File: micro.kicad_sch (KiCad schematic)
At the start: 23 parts, among them U10 RP2040, U11 W25Q128JVS, Y2 12MHz

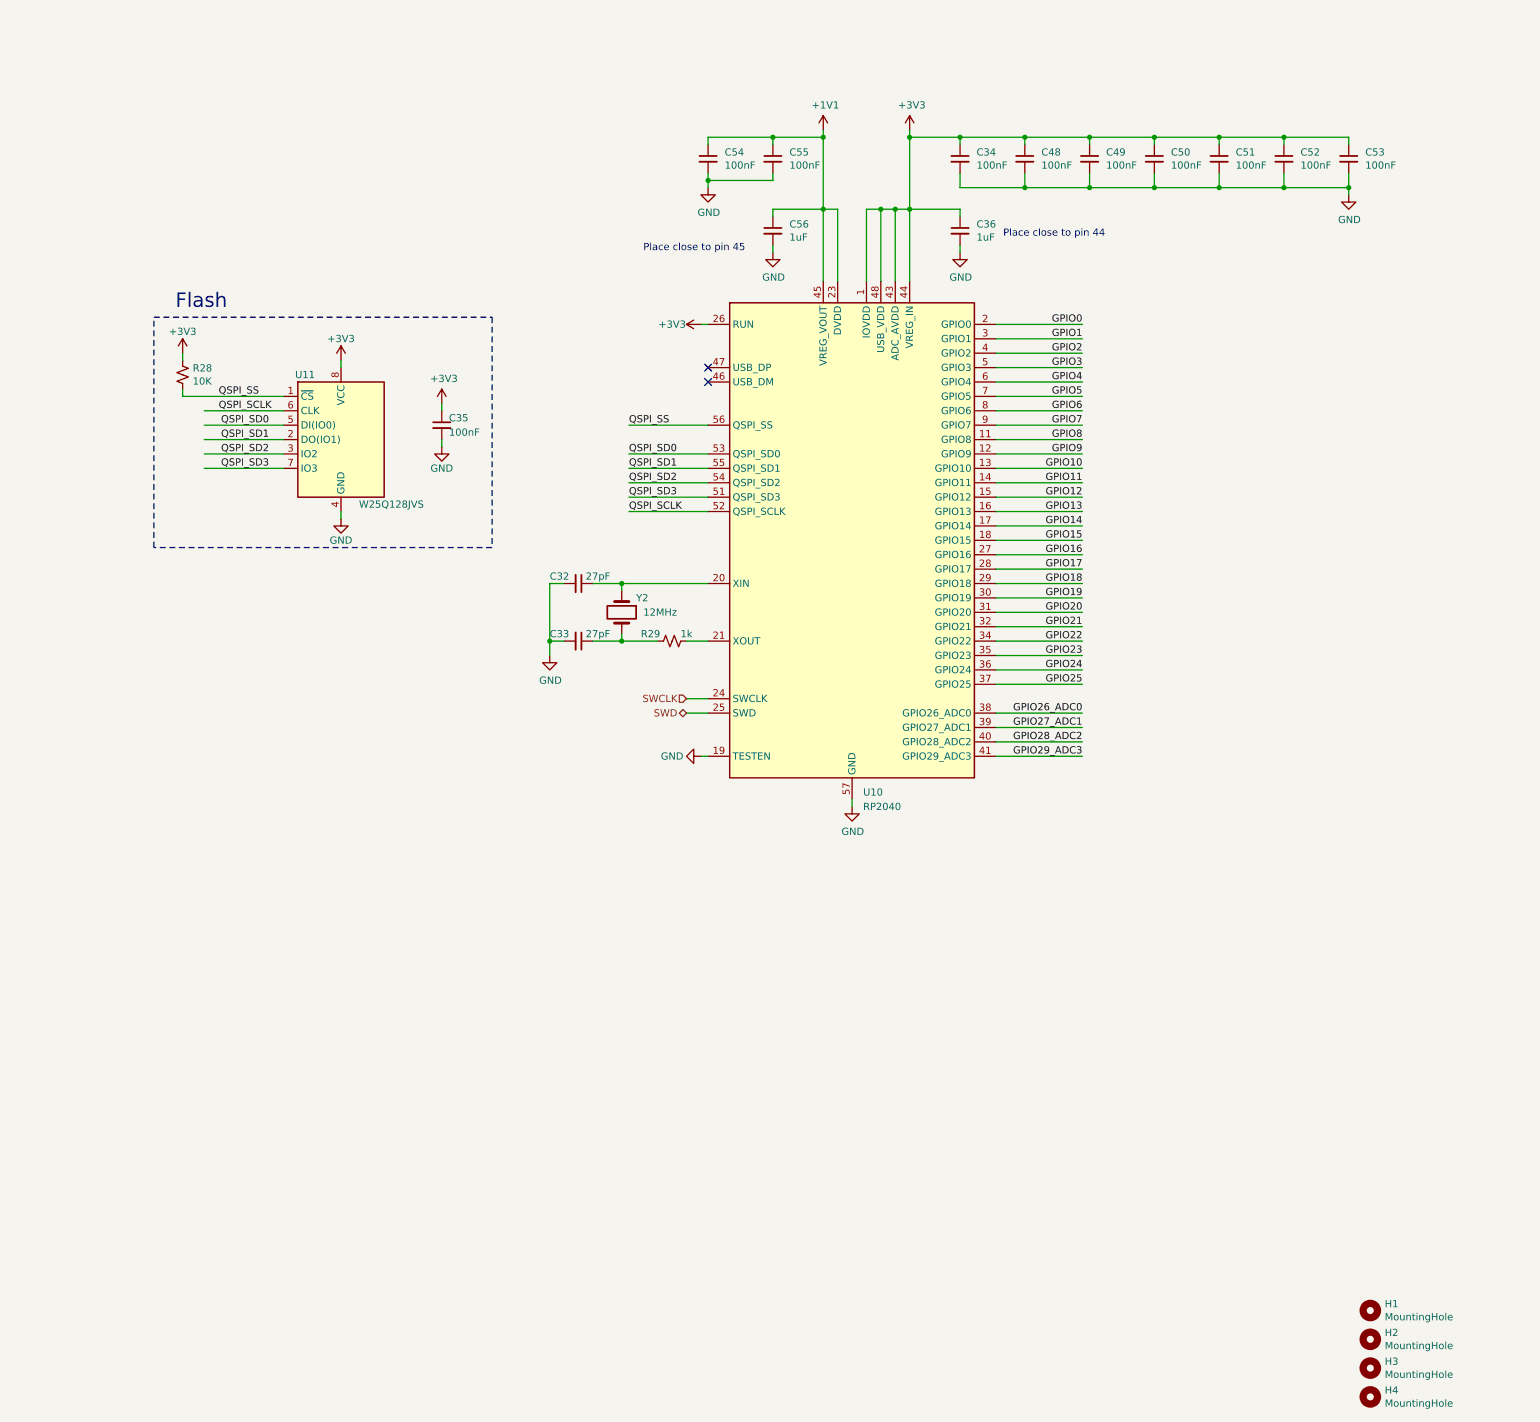
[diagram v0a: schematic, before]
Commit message: Finish RP2040 connections.
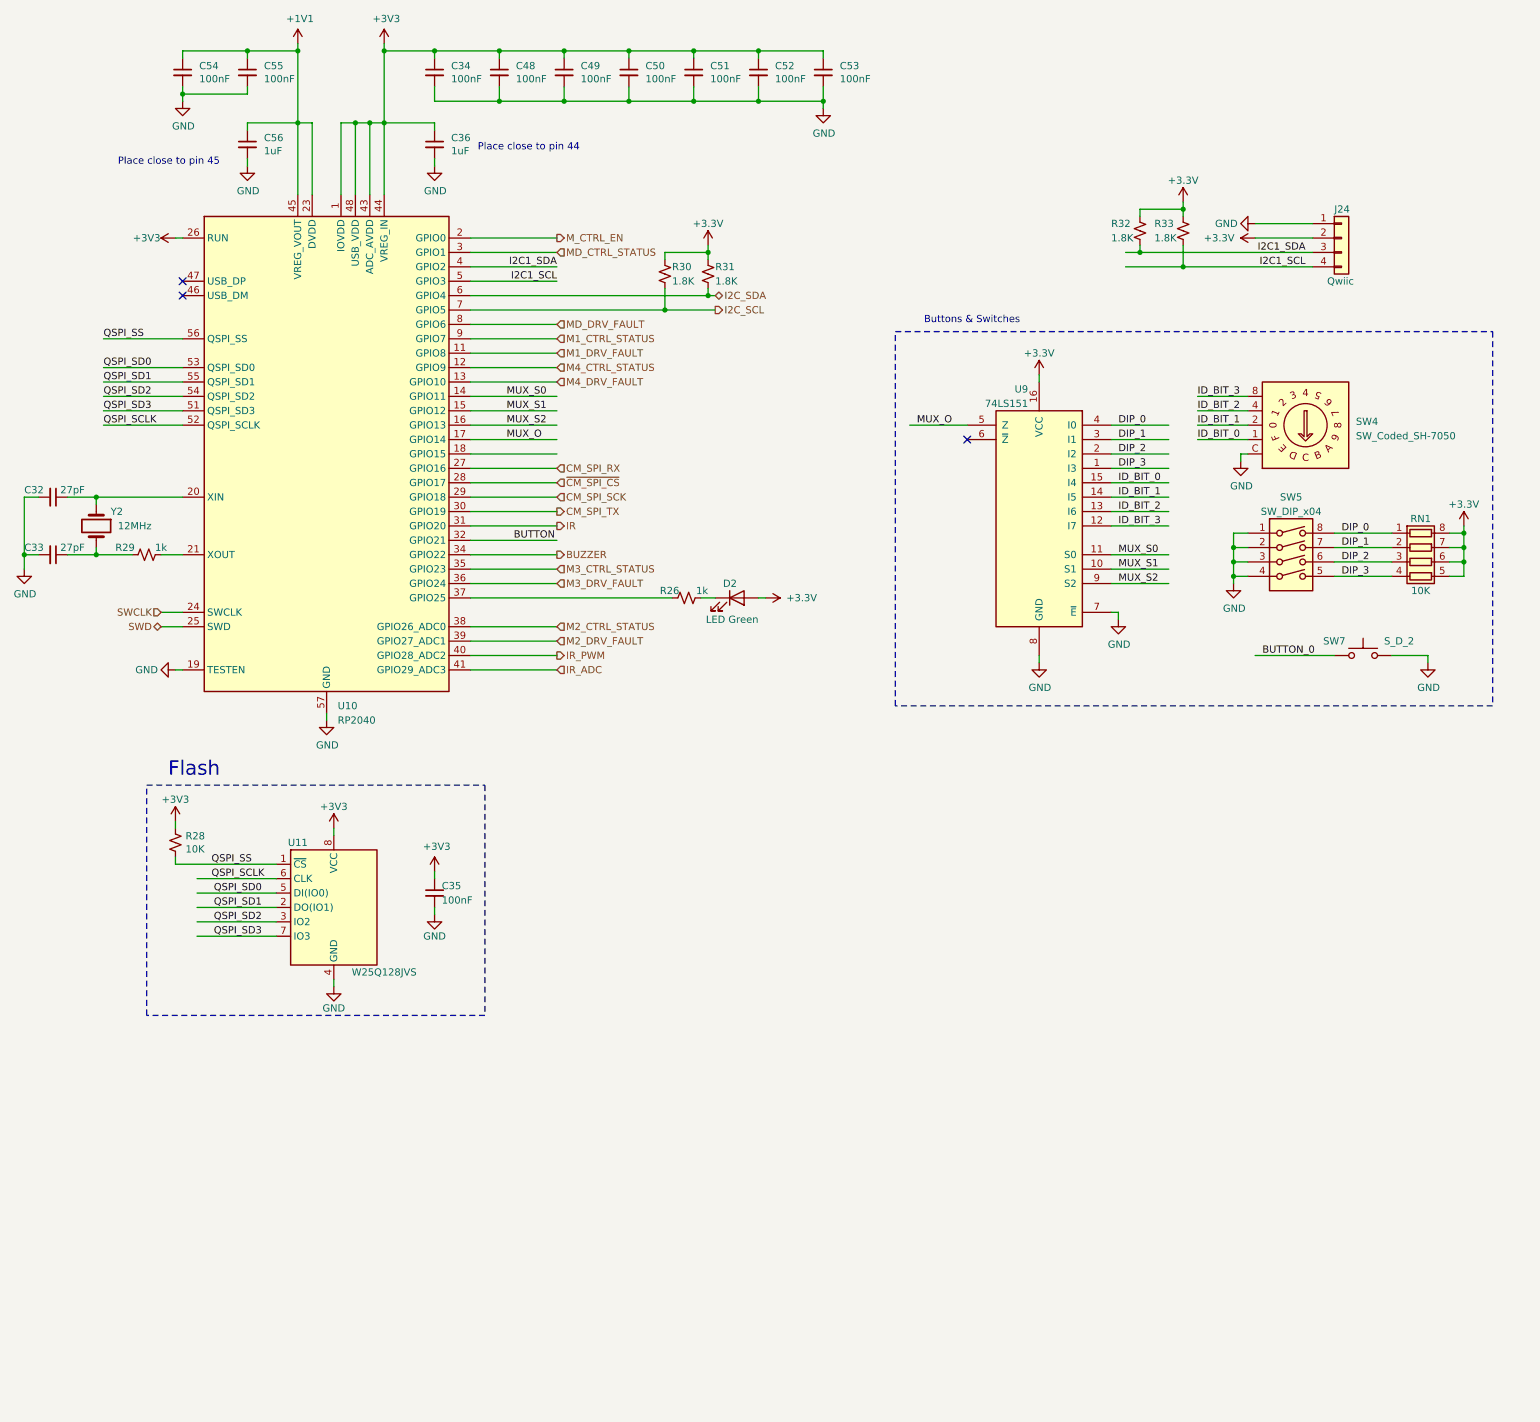
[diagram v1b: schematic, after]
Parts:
- removed H1, H2, H3, H4: MountingHole, MountingHole:MountingHole_2.7mm_M2.5, symbol Mechanical:MountingHole
- added D2: LED Green, LED_SMD:LED_0603_1608Metric, symbol Device:LED
- added J24: Qwiic, Connector_JST:JST_SH_SM04B-SRSS-TB_1x04-1MP_P1.00mm_Horizontal, symbol Connector_Generic:Conn_01x04
- added R26: 1k, Resistor_SMD:R_0402_1005Metric, symbol Device:R_Small_US
- added R30, R31, R32, R33: 1.8K, symbol Device:R_Small_US
- added RN1: 10K, symbol Device:R_Pack04
- added SW4: SW_Coded_SH-7050, Button_Switch_SMD:Nidec_Copal_SH-7010A, symbol Switch:SW_Coded_SH-7050
- added SW5: SW_DIP_x04, symbol Switch:SW_DIP_x04
- added SW7: S_D_2, symbol Switch:SW_Push
- added U9: 74LS151, Package_SO:SOIC-16_3.9x9.9mm_P1.27mm, symbol 74xx:74LS151
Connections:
- net GND: now also J24.1 (Pin_1), SW4.C, SW5.1, SW5.2, SW5.3, SW5.4, SW7.2, U9.7 (~{E}), U9.8 (GND)
- net GPIO0 renamed M_CTRL_EN
- net GPIO1 renamed MD_CTRL_STATUS
- net GPIO10 renamed M4_DRV_FAULT
- net GPIO11 renamed MUX_S0
- net MUX_S0: now also U9.11 (S0)
- net GPIO12 renamed MUX_S1
- net MUX_S1: now also U9.10 (S1)
- net GPIO13 renamed MUX_S2
- net MUX_S2: now also U9.9 (S2)
- net GPIO14 renamed MUX_O
- net MUX_O: now also U9.5 (Z)
- net GPIO15: no longer names the net of U10.18 (GPIO15)
- net GPIO16 renamed CM_SPI_RX
- net GPIO17 renamed ~{CM_SPI_CS}
- net GPIO18 renamed CM_SPI_SCK
- net GPIO19 renamed CM_SPI_TX
- net GPIO2 renamed I2C1_SDA
- net I2C1_SDA: now also J24.3 (Pin_3), R32.2
- net GPIO20 renamed IR
- net GPIO21 renamed BUTTON
- net GPIO22 renamed BUZZER
- net GPIO23 renamed M3_CTRL_STATUS
- net GPIO24 renamed M3_DRV_FAULT
- net GPIO25: no longer names the net of U10.37 (GPIO25)
- net GPIO25: now also R26.1
- net GPIO26_ADC0 renamed M2_CTRL_STATUS
- net GPIO27_ADC1 renamed M2_DRV_FAULT
- net GPIO28_ADC2 renamed IR_PWM
- net GPIO29_ADC3 renamed IR_ADC
- net GPIO3 renamed I2C1_SCL
- net I2C1_SCL: now also J24.4 (Pin_4), R33.2
- net GPIO4 renamed I2C_SDA
- net I2C_SDA: now also R31.2
- net GPIO5 renamed I2C_SCL
- net I2C_SCL: now also R30.2
- net GPIO6 renamed MD_DRV_FAULT
- net GPIO7 renamed M1_CTRL_STATUS
- net GPIO8 renamed M1_DRV_FAULT
- net GPIO9 renamed M4_CTRL_STATUS
- new net: D2.1 (K), R26.2
- new net +3.3V: D2.2 (A), J24.2 (Pin_2), R30.1, R31.1, R32.1, R33.1, RN1.5 (R4.2), RN1.6 (R3.2), RN1.7 (R2.2), RN1.8 (R1.2), U9.16 (VCC)
- new net BUTTON_0: SW7.1
- new net DIP_0: RN1.1 (R1.1), SW5.8, U9.4 (I0)
- new net DIP_1: RN1.2 (R2.1), SW5.7, U9.3 (I1)
- new net DIP_2: RN1.3 (R3.1), SW5.6, U9.2 (I2)
- new net DIP_3: RN1.4 (R4.1), SW5.5, U9.1 (I3)
- new net ID_BIT_0: SW4.1, U9.15 (I4)
- new net ID_BIT_1: SW4.2, U9.14 (I5)
- new net ID_BIT_2: SW4.4, U9.13 (I6)
- new net ID_BIT_3: SW4.8, U9.12 (I7)
- no-connect marks 2 -> 3
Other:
- note added: "Buttons & Switches"
- moved on the sheet: C32, C33, C34, C35, C36, C48, C49, C50, C51, C52, C53, C54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

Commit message: Finish connecting everything in sch.
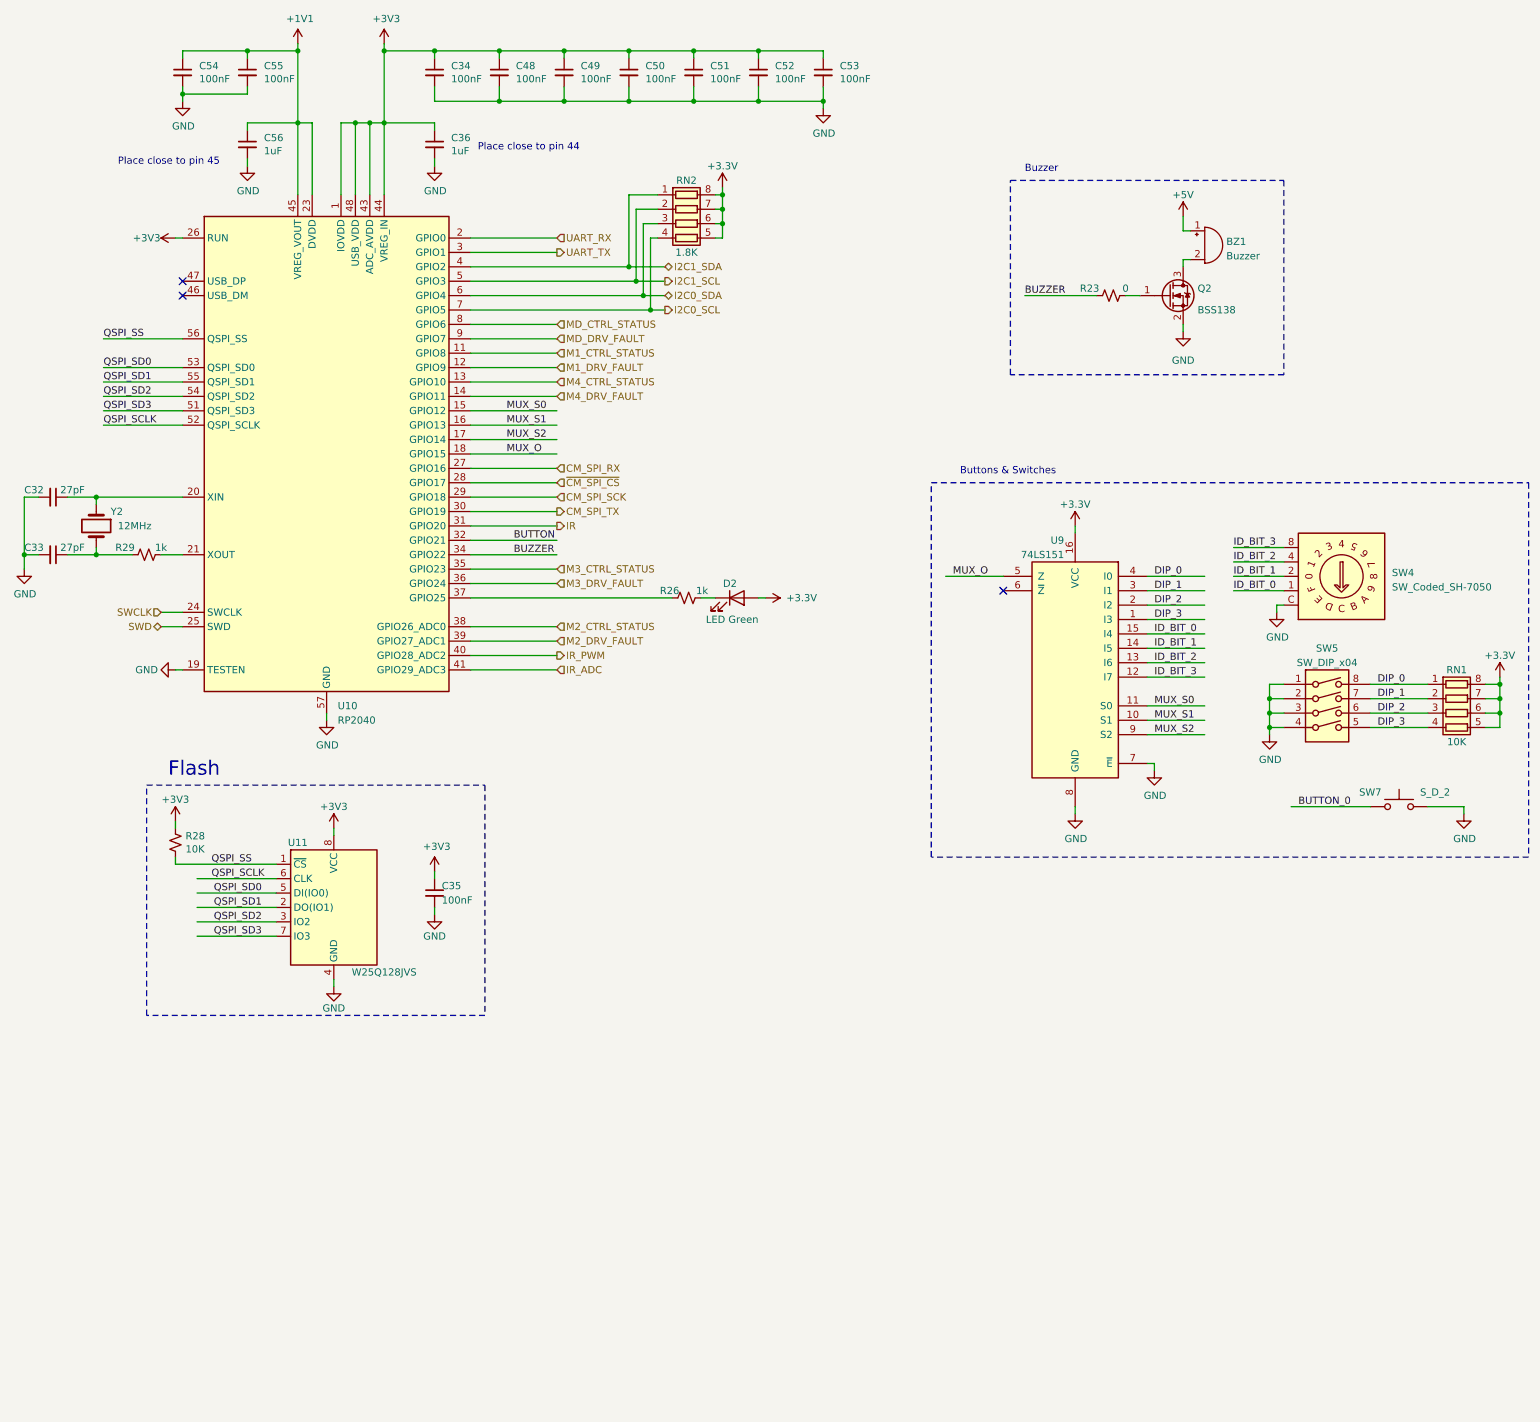
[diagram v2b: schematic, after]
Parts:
- removed J24: Qwiic, Connector_JST:JST_SH_SM04B-SRSS-TB_1x04-1MP_P1.00mm_Horizontal, symbol Connector_Generic:Conn_01x04
- removed R30, R31, R32, R33: 1.8K, symbol Device:R_Small_US
- added BZ1: Buzzer, Buzzer_Beeper:MagneticBuzzer_CUI_CMT-8504-100-SMT, symbol Device:Buzzer
- added Q2: BSS138, Package_TO_SOT_SMD:SOT-23, symbol Transistor_FET:BSS138
- added R23: 0, symbol Device:R_Small_US
- added RN2: 1.8K, symbol Device:R_Pack04
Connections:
- net +3.3V: now also RN2.5 (R4.2), RN2.6 (R3.2), RN2.7 (R2.2), RN2.8 (R1.2)
- net BUZZER: now also R23.1
- net GND: now also Q2.2 (S)
- net I2C1_SCL: now also RN2.2 (R2.1)
- net I2C1_SDA: now also RN2.1 (R1.1)
- net M1_CTRL_STATUS: now also U10.11 (GPIO8); no longer U10.9 (GPIO7)
- net M1_DRV_FAULT: now also U10.12 (GPIO9); no longer U10.11 (GPIO8)
- net M4_CTRL_STATUS: now also U10.13 (GPIO10); no longer U10.12 (GPIO9)
- net M4_DRV_FAULT: now also U10.14 (GPIO11); no longer U10.13 (GPIO10)
- net MD_CTRL_STATUS: now also U10.8 (GPIO6); no longer U10.3 (GPIO1)
- net MD_DRV_FAULT: now also U10.9 (GPIO7); no longer U10.8 (GPIO6)
- net MUX_O: now also U10.18 (GPIO15); no longer U10.17 (GPIO14)
- net MUX_S0: now also U10.15 (GPIO12); no longer U10.14 (GPIO11)
- net MUX_S1: now also U10.16 (GPIO13); no longer U10.15 (GPIO12)
- net MUX_S2: now also U10.17 (GPIO14); no longer U10.16 (GPIO13)
- net I2C_SCL renamed I2C0_SCL
- net I2C0_SCL: now also RN2.4 (R4.1)
- net I2C_SDA renamed I2C0_SDA
- net I2C0_SDA: now also RN2.3 (R3.1)
- net M_CTRL_EN renamed UART_RX
- new net: Q2.1 (G), R23.2
- new net: BZ1.2 (+), Q2.3 (D)
- new net +5V: BZ1.1 (-)
- new net UART_TX: U10.3 (GPIO1)
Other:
- note added: "Buzzer"
- moved on the sheet: RN1, SW4, SW5, SW7, U9

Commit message: Fix sch errors and warnings.
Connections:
- net BUTTON_0 is gone; now on net BUTTON: SW7.1
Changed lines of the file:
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@@
     (effects (font (size 1.27 1.27)) (justify left bottom))
   )
-  (label "BUTTON_0" (at 238.76 154.94 0) (fields_autoplaced)
+  (label "BUTTON" (at 238.76 154.94 0) (fields_autoplaced)
     (effects (font (size 1.27 1.27)) (justify left bottom))
   )
@@
       (effects (font (size 1.27 1.27)) hide)
     )
-    (property "Datasheet" "http://optoelectronics.liteon.com/upload/download/DS22-2000-226/LTST-S270KGKT.pdf" (at 139.7 118.11 0)
-      (effects (font (size 1.27 1.27)) hide)
-    )
+    (property "Datasheet" "~" (at 139.7 118.11 0)
+      (effects (font (size 1.27 1.27)) hide)
+    )

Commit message: Assign some of the footprints and MPNs.
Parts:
- D2: Field4 Digikey -> (none); Field5 LTST-S270KGKT -> (none); Field6 SML-A12M8TT86N -> (none); Field7 Rohm -> (none); Field8 650263301 -> (none); MPN (none) -> SML-A12M8TT86N; Part Description Green 572nm LED Indication - Discrete 2.2V 2-SMD, No Lead -> (none)
- R23: footprint (none) -> Resistor_SMD:R_0402_1005Metric
- R26: Field4 Farnell -> (none); Field5 9239235 -> (none); Field6 RK73H1ETTP1001F -> (none); Field7 KOA EUROPE GMBH -> (none); Field8 125049511 -> (none); MPN (none) -> RK73H1ETTP1001F; Part Description Resistor 1K M1005 1% 63mW -> (none)
- R28, R29: footprint Capacitor_SMD:C_0402_1005Metric -> Resistor_SMD:R_0402_1005Metric
- SW7: footprint (none) -> Button_Switch_SMD:SW_Push_1P1T_NO_6x6mm_H9.5mm
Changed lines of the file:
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@@
       (effects (font (size 1.27 1.27)) hide)
     )
-    (property "Field4" "Farnell" (at 130.81 118.11 0)
-      (effects (font (size 1.27 1.27)) hide)
-    )
-    (property "Field5" "9239235" (at 130.81 118.11 0)
-      (effects (font (size 1.27 1.27)) hide)
-    )
-    (property "Field7" "KOA EUROPE GMBH" (at 130.81 118.11 0)
-      (effects (font (size 1.27 1.27)) hide)
-    )
-    (property "Field6" "RK73H1ETTP1001F" (at 130.81 118.11 0)
-      (effects (font (size 1.27 1.27)) hide)
-    )
-    (property "Part Description" "Resistor 1K M1005 1% 63mW" (at 130.81 118.11 0)
-      (effects (font (size 1.27 1.27)) hide)
-    )
-    (property "Field8" "125049511" (at 130.81 118.11 0)
+    (property "MPN" "RK73H1ETTP1001F" (at 130.81 118.11 0)
       (effects (font (size 1.27 1.27)) hide)
     )
@@
       (effects (font (size 1.27 1.27)))
     )
-    (property "Footprint" "" (at 205.74 64.77 0)
+    (property "Footprint" "Resistor_SMD:R_0402_1005Metric" (at 205.74 64.77 0)
       (effects (font (size 1.27 1.27)) hide)
     )
@@
       (effects (font (size 1.27 1.27)) (justify left))
     )
-    (property "Footprint" "Capacitor_SMD:C_0402_1005Metric" (at 40.64 161.29 0)
+    (property "Footprint" "Resistor_SMD:R_0402_1005Metric" (at 40.64 161.29 0)
       (effects (font (size 1.27 1.27)) hide)
     )
@@
       (effects (font (size 1.27 1.27)))
     )
-    (property "Footprint" "Capacitor_SMD:C_0402_1005Metric" (at 35.56 110.49 0)
+    (property "Footprint" "Resistor_SMD:R_0402_1005Metric" (at 35.56 110.49 0)
       (effects (font (size 1.27 1.27)) hide)
     )
@@
       (effects (font (size 1.27 1.27)) hide)
     )
-    (property "Field4" "Digikey " (at 139.7 118.11 0)
-      (effects (font (size 1.27 1.27)) hide)
-    )
-    (property "Field5" "LTST-S270KGKT" (at 139.7 118.11 0)
-      (effects (font (size 1.27 1.27)) hide)
-    )
-    (property "Field6" "SML-A12M8TT86N" (at 139.7 118.11 0)
-      (effects (font (size 1.27 1.27)) hide)
-    )
-    (property "Field7" "Rohm" (at 139.7 118.11 0)
-      (effects (font (size 1.27 1.27)) hide)
-    )
-    (property "Field8" "650263301" (at 139.7 118.11 0)
-      (effects (font (size 1.27 1.27)) hide)
-    )
-    (property "Part Description" "	Green 572nm LED Indication - Discrete 2.2V 2-SMD, No Lead" (at 139.7 118.11 0)
+    (property "MPN" "SML-A12M8TT86N" (at 139.7 118.11 0)
       (effects (font (size 1.27 1.27)) hide)
     )
@@
       (effects (font (size 1.27 1.27)))
     )
-    (property "Footprint" "" (at 256.54 149.86 0)
-      (effects (font (size 1.27 1.27)) hide)
-    )
+    (property "Footprint" "Button_Switch_SMD:SW_Push_1P1T_NO_6x6mm_H9.5mm" (at 256.54 149.86 0)
+      (effects (font (size 1.27 1.27)) hide)
+    )
